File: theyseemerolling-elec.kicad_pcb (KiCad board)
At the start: 2 copper layers, 75 x 50 mm, 88 parts, among them IC2 L6205PD, J1 Conn_Encoder1, J2 Conn_Power_In, J3 Conn_SWD_UART, J4 Conn_Mot1, J5 Conn_Mot2, J6 Conn_Encoder2, J7 CAN_conn, J8 CAN_conn, Q1 BSS138, Q2 BSS138, Q3 BSS138, Q4 BSS138, Q5 BSS138, U1 STM32F303K8Tx, U2 LD1117S50TR_SOT223, U3 ACS711xLCTR-12AB, U4 ACS711xLCTR-12AB, U5 74HC00, U6 LD1117S33TR_SOT223, U7 TCAN332, U8 AT25SF041

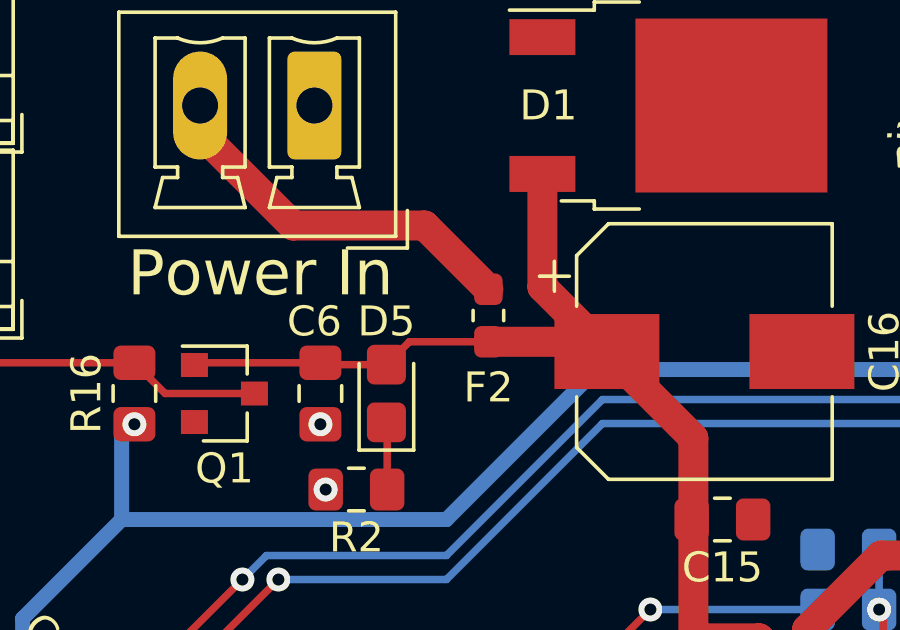
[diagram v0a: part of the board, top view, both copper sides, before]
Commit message: Changed fuse footprint
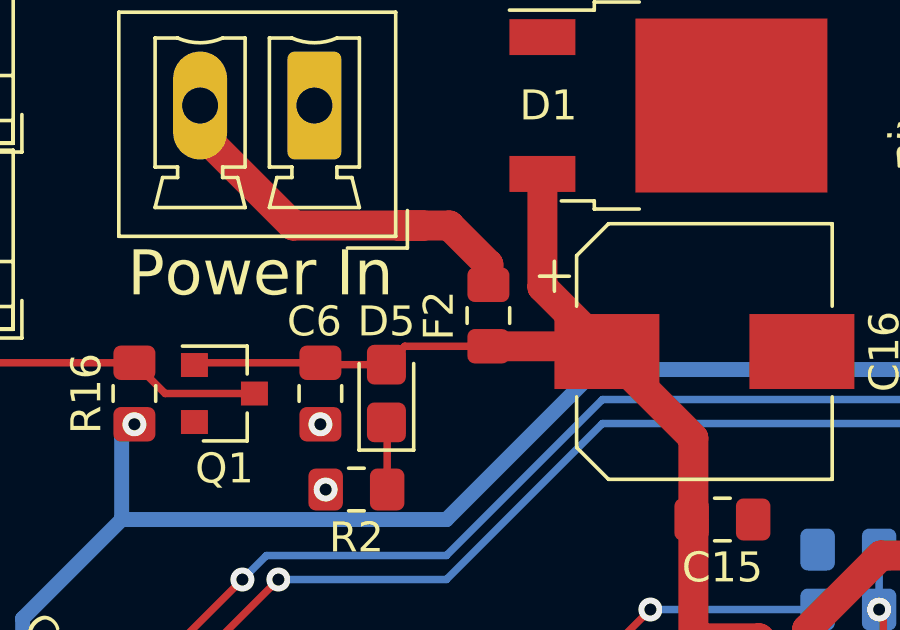
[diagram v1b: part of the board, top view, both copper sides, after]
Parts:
- F2: footprint Fuse:Fuse_0603_1608Metric_Pad1.05x0.95mm_HandSolder -> Fuse:Fuse_0805_2012Metric_Pad1.15x1.40mm_HandSolder
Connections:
- U1 pad 20: Net-(U1-Pad20) -> (no net)
- U7 pad 5: Net-(U7-Pad5) -> (no net)
- U7 pad 8: Net-(U7-Pad8) -> (no net)
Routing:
- net Net-(F2-Pad2): track 13.6 -> 14.8 mm

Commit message: Fix footprint on pcb
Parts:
- moved D5 2.24 mm to (134.6, 64.2)
- moved Q1 2.24 mm to (129.2, 64.2)
- moved R2 2.24 mm to (133.6, 67.4)
- moved R16 2.24 mm to (126.2, 64.2)
- moved C6 2.24 mm to (132.4, 64.2)
- moved F2 0.57 mm to (139.8, 61.6), turned to 180 degrees
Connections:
- U1 pad 20: (no net) -> Net-(U1-Pad20)
- U7 pad 5: (no net) -> Net-(U7-Pad5)
- U7 pad 8: (no net) -> Net-(U7-Pad8)
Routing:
- net +3V3: track 209.0 -> 211.6 mm
- net Net-(F2-Pad2): track 14.8 -> 12.3 mm
- net /f3/ABOUT_DA_POWER: track 32.4 -> 30.4 mm
- net VCC: track 62.2 -> 62.9 mm

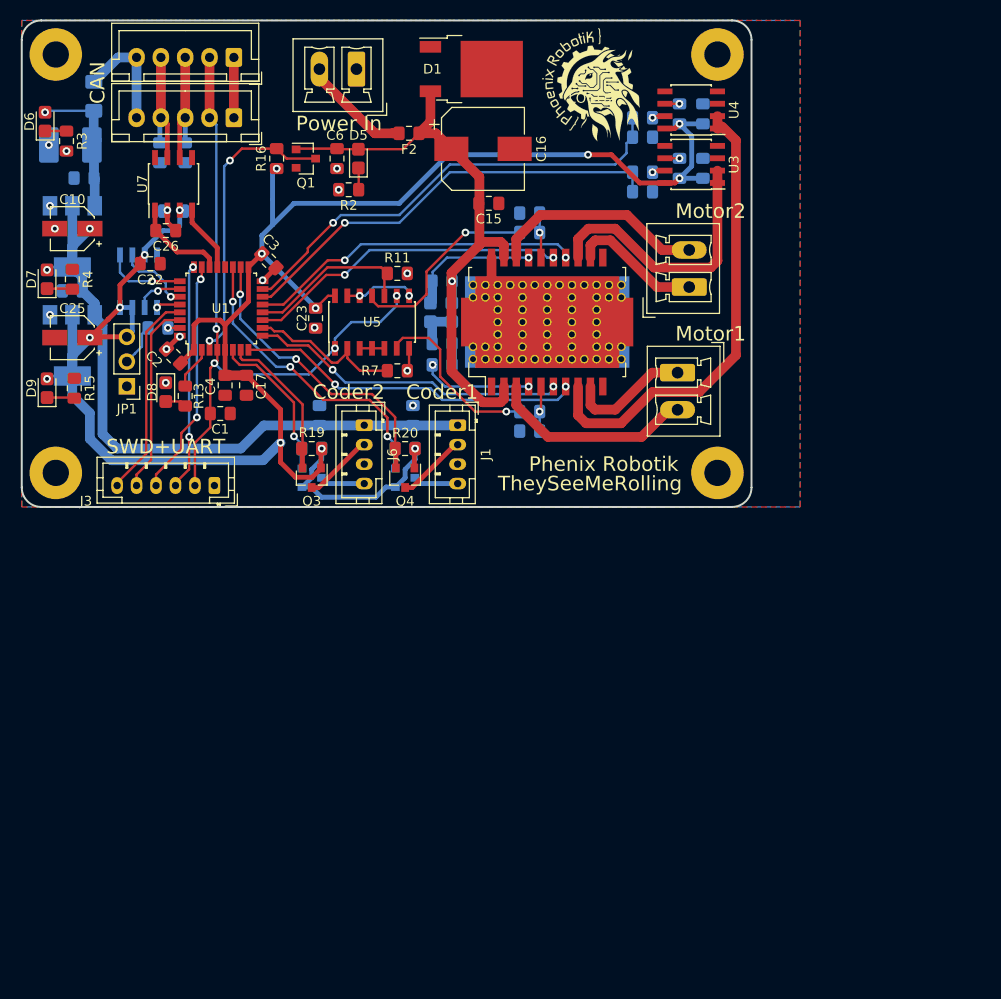
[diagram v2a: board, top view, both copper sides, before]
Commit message: Rework the schematics. Destroy the pcb. re-annotated the schematics.
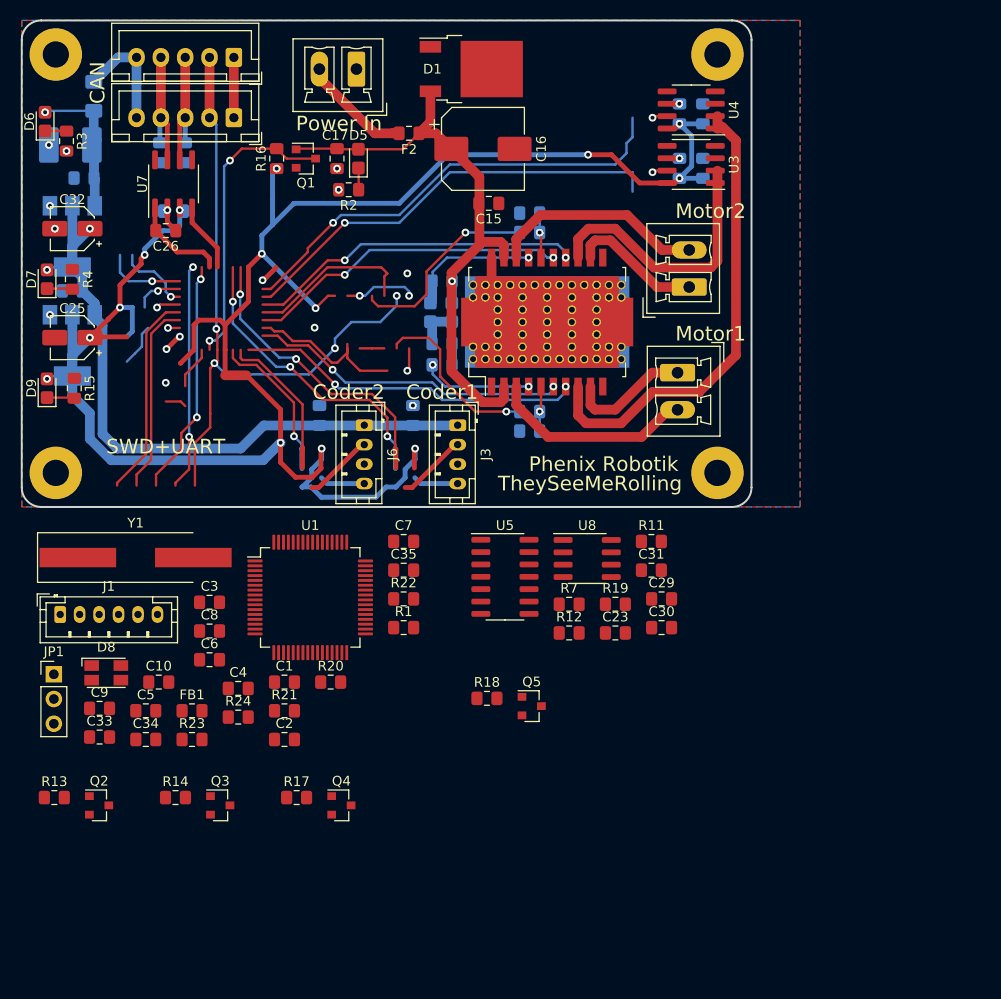
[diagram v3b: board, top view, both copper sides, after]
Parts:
- removed the C17 at (123.1, 87.5)
- removed the C22 at (113.2, 75.0)
- removed the J3 at (119.8, 97.8)
- removed LOGO1: Logo_Open_Hardware_Large, Symbol:OSHW-Logo_7.5x8mm_SilkScreen
- removed LOGO2: Logo_Open_Hardware_Small, PhenixRobotik:Logo_14,5mm
- added C10: 2u2, Capacitor_SMD:C_0805_2012Metric_Pad1.15x1.40mm_HandSolder, F.Cu at (114.1, 118.0)
- added C29: 1n, Capacitor_SMD:C_0805_2012Metric_Pad1.15x1.40mm_HandSolder, F.Cu at (165.8, 109.5)
- added C30: 100nF, Capacitor_SMD:C_0805_2012Metric_Pad1.15x1.40mm_HandSolder, F.Cu at (165.8, 112.4)
- added C31: 100nF, Capacitor_SMD:C_0805_2012Metric_Pad1.15x1.40mm_HandSolder, F.Cu at (164.7, 106.5)
- added C33: 2u2, Capacitor_SMD:C_0805_2012Metric_Pad1.15x1.40mm_HandSolder, F.Cu at (108.0, 123.7)
- added C34: C, Capacitor_SMD:C_0805_2012Metric_Pad1.15x1.40mm_HandSolder, F.Cu at (112.8, 123.9)
- added C35: C, Capacitor_SMD:C_0805_2012Metric_Pad1.15x1.40mm_HandSolder, F.Cu at (139.2, 106.5)
- added C5: 100n, Capacitor_SMD:C_0805_2012Metric_Pad1.15x1.40mm_HandSolder, F.Cu at (112.8, 121.0)
- added C6: 4.7u -- 10u, Capacitor_SMD:C_0805_2012Metric_Pad1.15x1.40mm_HandSolder, F.Cu at (119.3, 115.7)
- added C7: 100n, Capacitor_SMD:C_0805_2012Metric_Pad1.15x1.40mm_HandSolder, F.Cu at (139.2, 103.5)
- added FB1: Ferrite_Bead, Inductor_SMD:L_0805_2012Metric_Pad1.15x1.40mm_HandSolder, F.Cu at (117.5, 121.0)
- added J1: Conn_Debug, Connector_JST:JST_PH_B6B-PH-K_1x06_P2.00mm_Vertical, F.Cu at (104.0, 111.0)
- added R17: R, Resistor_SMD:R_0805_2012Metric_Pad1.15x1.40mm_HandSolder, F.Cu at (128.2, 129.9)
- added R22: 1k, Resistor_SMD:R_0805_2012Metric_Pad1.15x1.40mm_HandSolder, F.Cu at (139.2, 109.5)
- added R23: 1k, Resistor_SMD:R_0805_2012Metric_Pad1.15x1.40mm_HandSolder, F.Cu at (117.5, 123.9)
- added R24: 1k, Resistor_SMD:R_0805_2012Metric_Pad1.15x1.40mm_HandSolder, F.Cu at (122.2, 121.6)
- added Y1: 8Mhz, Crystal:Crystal_SMD_HC49-SD_HandSoldering, F.Cu at (111.7, 105.2)
- C23: value 100nF -> 1n
- C8: value 1n -> 1u; moved to F.Cu
- C9: value 1n -> 100n; moved to F.Cu
- D8: value LED_ALT -> LED_CRGB; footprint LED_SMD:LED_0805_2012Metric_Castellated -> LED_SMD:LED_Avago_PLCC4_3.2x2.8mm_CW
- Q2, Q5, R18, R21, U8: moved to F.Cu
- R1: value 10kR -> 10k; moved to F.Cu
- R11: value 10kR -> Rsense
- R12: value R_Sense -> Rsense; moved to F.Cu
- R13: value 1kR -> R
- R14: value R_Sense -> R; moved to F.Cu
- R19: value R -> 10kR
- U1: value STM32F303K8Tx -> STM32F405RGTx; footprint Package_QFP:LQFP-32_7x7mm_P0.8mm -> Package_QFP:LQFP-64_10x10mm_P0.5mm
- moved R14 84.8 mm to (115.8, 129.9), turned to 0 degrees
- moved C9 81.0 mm to (108.0, 120.7)
- moved C8 63.4 mm to (119.3, 112.8)
- moved U8 54.2 mm to (158.1, 105.3), turned to 0 degrees
- moved R12 47.9 mm to (156.3, 113.0), turned to 0 degrees
- moved C23 44.7 mm to (161.0, 113.0), turned to 0 degrees
- moved R13 43.4 mm to (103.3, 129.9), turned to 0 degrees
- moved C2 41.0 mm to (127.0, 123.9), turned to 0 degrees
- moved Q2 40.1 mm to (108.0, 130.7)
- moved R1 39.8 mm to (139.2, 112.4), turned to 0 degrees
- moved R11 38.0 mm to (164.7, 103.5)
- moved C3 35.6 mm to (119.3, 109.8), turned to 0 degrees
- moved R19 35.1 mm to (161.0, 110.0)
- moved Q3 35.0 mm to (120.4, 130.7), turned to 0 degrees
- moved Q4 34.3 mm to (132.8, 130.7), turned to 0 degrees
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- renumbered C6 to C17, C5 to C22, C10 to C32, C7 to C36, J1 to J3
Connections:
- net /DualDCDriver/Sense_B renamed /Sense_B
- net /f3/Encoder_1_B renamed /shift_enc1B/Input
- net /f3/Encoder_2_A renamed /shift_enc2A/Input
- C1 pad 2: /CAN/NRST -> +3V3
- C2 pad 1: +3V3 -> GND
- C2 pad 2: GND -> +3V3
- C23 pad 1: +3V3 -> /Sense_A_Filtered
- C26 pad 1: /f3/CAN_TX -> /CAN/CAN_TX
- C3 pad 1: +3V3 -> GND
- C3 pad 2: GND -> +3V3
- C4 pad 1: +3V3 -> GND
- C4 pad 2: GND -> +3V3
- C8 pad 1: /f3/Sense_B_Filtered -> GND
- C8 pad 2: GND -> VDDA
- C9 pad 1: /f3/Sense_A_Filtered -> GND
- C9 pad 2: GND -> /stm32f4/nrst
- J3 pad 2: /f3/Encoder_1_A -> /shift_enc1A/Input
- J6 pad 4: /f3/Encoder_2_B -> /shift_enc2B/Input
- Q1 pad 3: /f3/ABOUT_DA_POWER -> /stm32f4/~AboutDaPower
- Q2 pad 2: Net-(Q2-Pad2) -> /stm32f4/Encoder_1_B
- Q2 pad 3: /f3/Encoder_2_B -> /shift_enc1A/Input
- Q3 pad 2: Net-(Q3-Pad2) -> /stm32f4/Encoder_2_A
- Q4 pad 2: Net-(Q4-Pad2) -> /stm32f4/Encoder_2_B
- Q4 pad 3: /f3/Encoder_1_A -> /shift_enc2B/Input
- Q5 pad 2: Net-(Q5-Pad2) -> /stm32f4/Encoder_1_A
- R11 pad 1: /f3/EN_B_and_NRST -> /Sense_A
- R11 pad 2: GND -> /Sense_A_Filtered
- R12 pad 2: /f3/Sense_B_Filtered -> /Sense_B_Filtered
- R13 pad 1: Net-(D8-Pad2) -> +3V3
- R13 pad 2: Net-(R13-Pad2) -> /stm32f4/Encoder_1_B
- R14 pad 1: /DualDCDriver/Sense_A -> +3V3
- R14 pad 2: /f3/Sense_A_Filtered -> /stm32f4/Encoder_2_A
- R16 pad 2: /f3/ABOUT_DA_POWER -> /stm32f4/~AboutDaPower
- R18 pad 2: Net-(Q2-Pad2) -> /stm32f4/Encoder_1_A
- R19 pad 1: Net-(Q3-Pad2) -> GND
- R19 pad 2: +3V3 -> /EN_A_and_NRST
- R20 pad 1: +3V3 -> Net-(R20-Pad1)
- R20 pad 2: Net-(Q4-Pad2) -> Net-(C34-Pad1)
- R21 pad 1: Net-(Q5-Pad2) -> Net-(R21-Pad1)
- R21 pad 2: +3V3 -> Net-(C35-Pad1)
- R7 pad 1: GND -> /EN_B_and_NRST
- R7 pad 2: /f3/EN_A_and_NRST -> GND
- U1 pad 10: /f3/EN_A_and_NRST -> (no net)
- U1 pad 11: /DualDCDriver/IN2_B -> (no net)
- U1 pad 12: /f3/EN_B_and_NRST -> GND
- U1 pad 13: /DualDCDriver/IN1_B -> VDDA
- U1 pad 14: /f3/Sense_B_Filtered -> /stm32f4/Encoder_2_A
- U1 pad 15: /f3/Sense_A_Filtered -> /stm32f4/Encoder_2_B
- U1 pad 16: GND -> (no net)
- U1 pad 17: +3V3 -> (no net)
- U1 pad 18: Net-(Q4-Pad2) -> GND
- U1 pad 19: Net-(Q5-Pad2) -> +3V3
- U1 pad 2: Net-(R13-Pad2) -> (no net)
- U1 pad 20: Net-(U1-Pad20) -> (no net)
- U1 pad 21: /f3/CAN_RX -> /DualDCDriver/IN2_A
- U1 pad 22: /f3/CAN_TX -> /DualDCDriver/IN1_A
- U1 pad 23: /f3/TMS -> /DualDCDriver/EN_A
- U1 pad 24: /f3/TCK -> /Sense_A_Filtered
- U1 pad 25: Net-(U1-Pad25) -> /Sense_B_Filtered
- U1 pad 26: /f3/SCK -> /DualDCDriver/IN1_B
- U1 pad 27: /f3/MISO -> /DualDCDriver/EN_B
- U1 pad 28: /f3/MOSI -> /DualDCDriver/IN2_B
- U1 pad 29: /f3/TX_1 -> (no net)
- U1 pad 3: /f3/ABOUT_DA_POWER -> (no net)
- U1 pad 30: /f3/RX_1 -> (no net)
- U1 pad 31: Net-(R1-Pad1) -> Net-(C10-Pad1)
- U1 pad 32: GND -> +3V3
- U1 pad 4: /CAN/NRST -> (no net)
- U1 pad 5: +3V3 -> Net-(R20-Pad1)
- U1 pad 6: Net-(Q2-Pad2) -> Net-(R21-Pad1)
- U1 pad 7: Net-(Q3-Pad2) -> /stm32f4/nrst
- U1 pad 8: /DualDCDriver/IN2_A -> (no net)
- U1 pad 9: /DualDCDriver/IN1_A -> (no net)
- U4 pad 7: /DualDCDriver/Sense_A -> /Sense_A
- U5 pad 1: /CAN/NRST -> /nrst
- U5 pad 10: /f3/EN_B_and_NRST -> /EN_B_and_NRST
- U5 pad 11: /DualDCDriver/EN_B -> (no net)
- U5 pad 2: /f3/EN_A_and_NRST -> /EN_A_and_NRST
- U5 pad 6: /DualDCDriver/EN_A -> (no net)
- U5 pad 9: /CAN/NRST -> /nrst
- U7 pad 1: /f3/CAN_TX -> /CAN/CAN_TX
- U7 pad 4: /f3/CAN_RX -> /CAN/CAN_RX
- U7 pad 5: Net-(U7-Pad5) -> (no net)
- U7 pad 8: Net-(U7-Pad8) -> (no net)
- U8 pad 1: Net-(U1-Pad25) -> (no net)
- U8 pad 2: /f3/MISO -> (no net)
- U8 pad 5: /f3/MOSI -> (no net)
- U8 pad 6: /f3/SCK -> (no net)
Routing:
- net /stm32f4/~AboutDaPower: track 0.00 -> 30.4 mm, vias 0 -> 2
- net /f3/ABOUT_DA_POWER: track 30.4 -> 0.00 mm, vias 2 -> 0
- net /f3/CAN_TX: track 9.74 -> 0.00 mm
- net /CAN/CAN_TX: track 0.00 -> 9.74 mm
- net /shift_enc1A/Input: track 0.00 -> 7.22 mm
- net /f3/Encoder_1_A: track 7.22 -> 0.00 mm
- net /f3/CAN_RX: track 6.92 -> 0.00 mm
- net /CAN/CAN_RX: track 0.00 -> 6.92 mm
- net /shift_enc2B/Input: track 0.00 -> 4.65 mm
- net /f3/Encoder_2_B: track 4.65 -> 0.00 mm
- net /Sense_A: track 0.00 -> 1.34 mm, vias 0 -> 1
- net /DualDCDriver/Sense_A: track 1.34 -> 0.00 mm, vias 1 -> 0

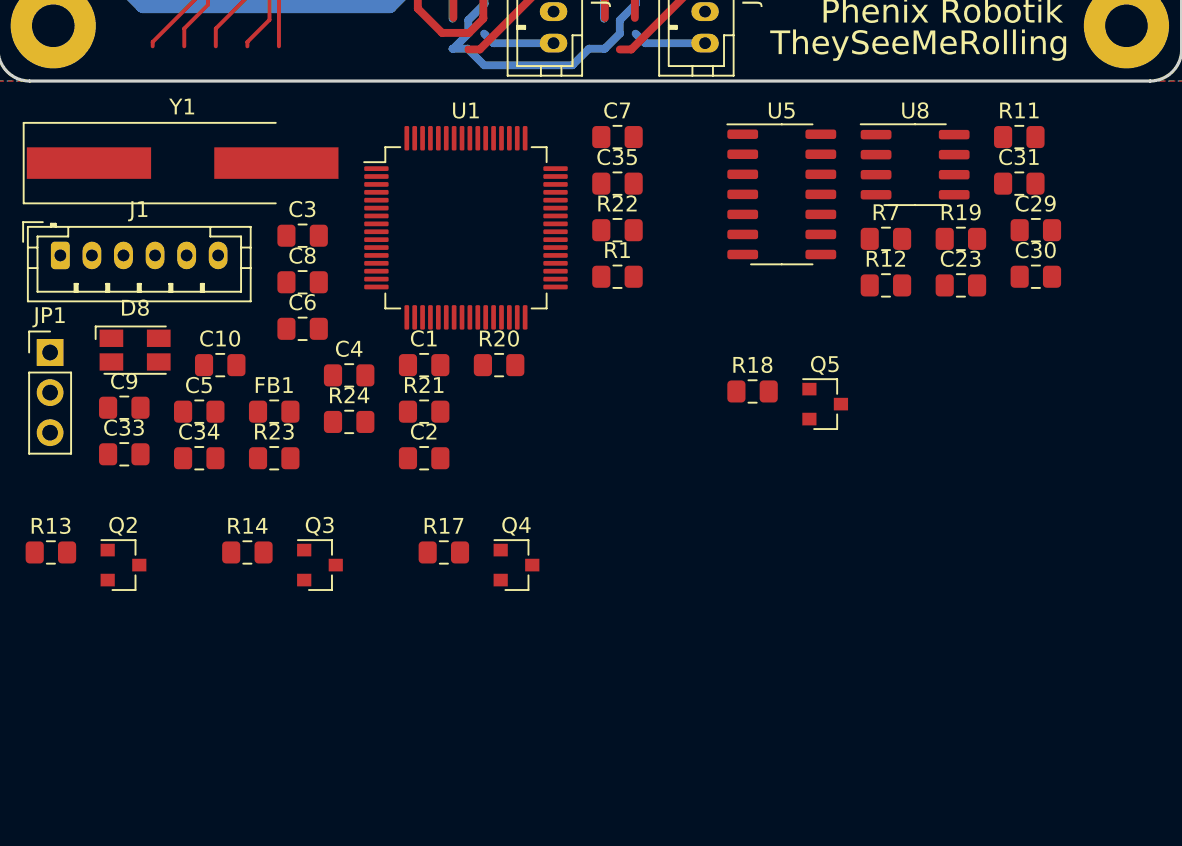
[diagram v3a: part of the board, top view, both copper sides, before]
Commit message: add correct rgb led
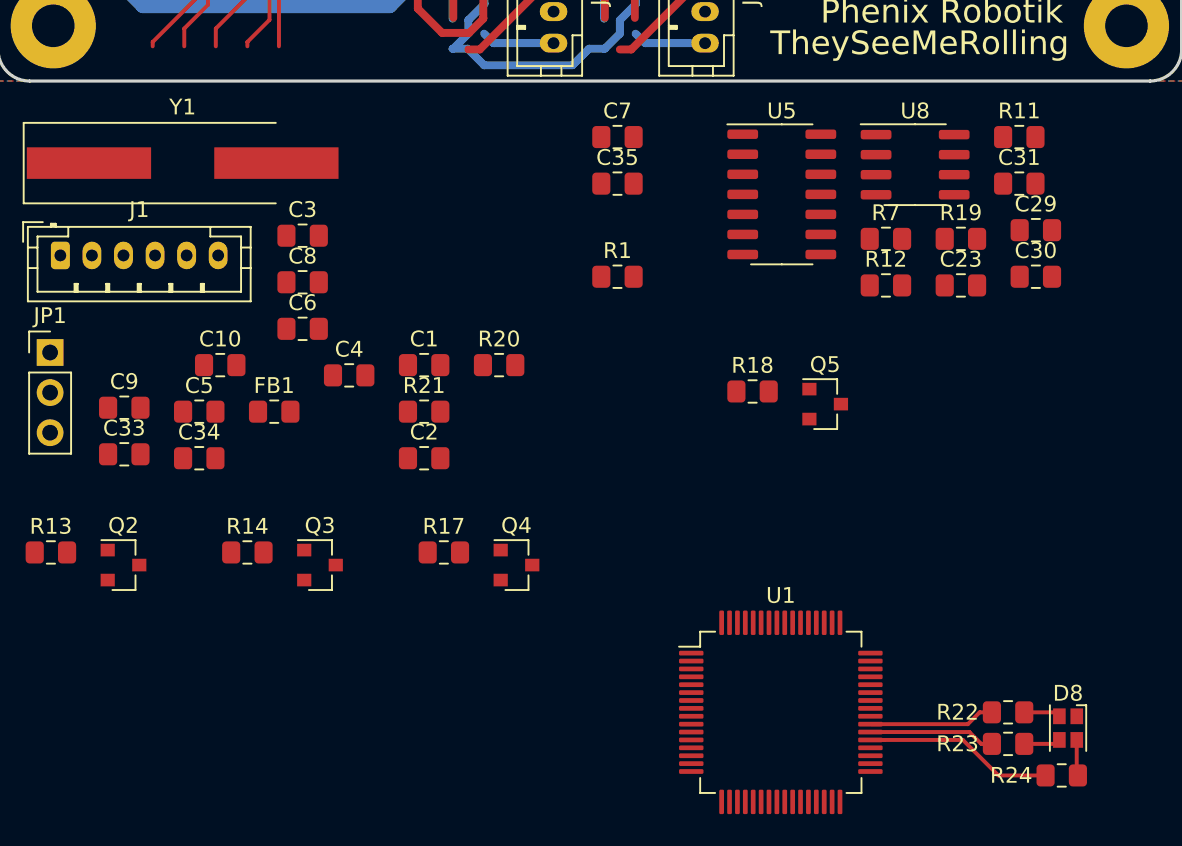
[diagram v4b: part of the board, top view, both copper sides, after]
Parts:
- D8: value LED_CRGB -> LED_ARGB; footprint LED_SMD:LED_Avago_PLCC4_3.2x2.8mm_CW -> LED_SMD:LED_Cree-PLCC4_2x2mm_CW
- R22: value 1k -> 39
- R23: value 1k -> 27
- R24: value 1k -> 91
- moved D8 63.8 mm to (167.8, 141.0), turned to 270 degrees
- moved R24 50.4 mm to (167.4, 144.0), turned to 180 degrees
- moved R23 49.9 mm to (164.0, 142.0), turned to 180 degrees
- moved R22 39.3 mm to (164.0, 140.0), turned to 180 degrees
- moved U1 36.6 mm to (149.6, 140.0)
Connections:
- D8 pad 1: GND -> +3V3
- R22 pad 1: Net-(D8-Pad2) -> Net-(D8-Pad4)
- R24 pad 1: Net-(D8-Pad4) -> Net-(D8-Pad2)
- U1 pad 37: Net-(R22-Pad2) -> Net-(R24-Pad2)
- U1 pad 39: Net-(R24-Pad2) -> Net-(R22-Pad2)
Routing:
- net Net-(R24-Pad2): track 0.00 -> 12.0 mm
- net Net-(R23-Pad2): track 0.00 -> 8.01 mm
- net Net-(R22-Pad2): track 0.00 -> 8.01 mm
- net Net-(D8-Pad4): track 0.00 -> 2.33 mm
- net Net-(D8-Pad3): track 0.00 -> 2.33 mm
- net Net-(D8-Pad2): track 2.19 -> 4.47 mm

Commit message: continue stm32f405
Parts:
- added C37: 1n, Capacitor_SMD:C_0805_2012Metric_Pad1.15x1.40mm_HandSolder, F.Cu at (188.4, 61.2)
- added R25: Rsense, Resistor_SMD:R_0805_2012Metric_Pad1.15x1.40mm_HandSolder, F.Cu at (196.9, 61.2)
- C1, C10, C2, C33, C34, C35, C5, C7: footprint Capacitor_SMD:C_0805_2012Metric_Pad1.15x1.40mm_HandSolder -> Capacitor_SMD:C_0603_1608Metric_Pad1.05x0.95mm_HandSolder
- C3, C4, C6, C8, C9: footprint Capacitor_SMD:C_0805_2012Metric_Pad1.15x1.40mm_HandSolder -> Capacitor_SMD:C_0603_1608Metric_Pad1.05x0.95mm_HandSolder; moved to B.Cu
- FB1: moved to B.Cu
- R1, R20, R21: footprint Resistor_SMD:R_0805_2012Metric_Pad1.15x1.40mm_HandSolder -> Resistor_SMD:R_0603_1608Metric_Pad1.05x0.95mm_HandSolder
- R5, R6: value 10kR -> 10k
- moved C3 46.3 mm to (151.6, 143.0)
- moved C8 40.4 mm to (146.8, 142.4), turned to 90 degrees
- moved C6 40.4 mm to (151.6, 140.0)
- moved C9 40.0 mm to (139.8, 145.0)
- moved Y1 39.6 mm to (133.2, 138.5), turned to 270 degrees
- moved C7 38.5 mm to (141.7, 142.0), turned to 270 degrees
- moved C35 36.1 mm to (137.6, 142.6), turned to 270 degrees
- moved C4 34.6 mm to (151.8, 136.6)
- moved FB1 33.8 mm to (146.8, 137.8), turned to 270 degrees
- moved C5 33.7 mm to (144.3, 132.7), turned to 270 degrees
- moved C2 30.4 mm to (145.6, 148.0)
- moved C34 27.0 mm to (137.6, 134.4), turned to 90 degrees
- moved R21 23.0 mm to (140.8, 139.3), turned to 180 degrees
- moved C1 22.3 mm to (142.6, 133.9), turned to 270 degrees
- moved R20 21.7 mm to (140.8, 137.7), turned to 180 degrees
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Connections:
- net /Sense_B renamed Net-(R12-Pad1)
- net Net-(IC2-Pad13) renamed /DualDCDriver/sheet5D55A35B/Input
- net Net-(IC2-Pad8) renamed /DualDCDriver/Sheet5D536196/Input
- C23 pad 1: /Sense_A_Filtered -> /DualDCDriver/Sense_B
- C29 pad 1: /Sense_B_Filtered -> /DualDCDriver/Sense_A
- R11 pad 1: /Sense_A -> /DualDCDriver/Sense_A
- R11 pad 2: /Sense_A_Filtered -> /DualDCDriver/Sense_A_Filtered
- R12 pad 2: /Sense_B_Filtered -> /DualDCDriver/Sense_B
- U1 pad 24: /Sense_A_Filtered -> /DualDCDriver/Sense_A
- U1 pad 25: /Sense_B_Filtered -> /DualDCDriver/Sense_B
- U4 pad 7: /Sense_A -> Net-(R25-Pad1)
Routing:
- net +3V3: track 211.6 -> 234.3 mm, vias 14 -> 17
- net VDDA: track 0.00 -> 8.27 mm, vias 0 -> 1
- net Net-(C34-Pad1): track 0.00 -> 6.78 mm
- net Net-(C35-Pad1): track 0.00 -> 6.66 mm
- net GND: track 18.4 -> 24.6 mm
- net Net-(R21-Pad1): track 0.00 -> 2.48 mm
- net Net-(R20-Pad1): track 0.00 -> 2.48 mm
- net Net-(R25-Pad1): track 0.00 -> 1.34 mm, vias 0 -> 1
- net /Sense_A: track 1.34 -> 0.00 mm, vias 1 -> 0
